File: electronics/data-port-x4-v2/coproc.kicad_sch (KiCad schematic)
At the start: 43 parts, among them U11 RP2354B, U12 AP2112K-3.3TRG1, Y2 ABM8-272-T3

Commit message: DATA x4 v2: the H5VU25UC ESD and 22 ohm USB resistors, two extended types fewer, re-routed
The user's "essaie les 3 premiers ?", via the orchestrator: two part
swaps, each an extended part type less in the panel order.

- R23/R24, the RP2354B's USB series resistors: 27 ohm (C25100,
  extended) -> 22 ohm 0402 (C25092, basic).  The RP2350's USB is Full
  Speed only: its driver's own impedance plus 22 ohm stays inside USB's
  28-44 ohm driver window, nearer its middle than 33 ohm.  Said in
  design.py.
- U4, U105...U406, the nine 4-line ESD arrays: TI TPD4E05U06DQAR
  (C138714) -> hongjiacheng H5VU25UC (C20615800, JLC "preferred
  extended": no Economic fee; $0.03 against $0.08).
  - On its own DFN2510-10L land (the tools commit before this).
  - The same pins; its 6/7/9/10 are tied inside to 5/4/2/1, so the
    flow-through lines keep one signal.
  - Its stand-off is 5 V (TI's 5.5 V).  Every line it guards stays at
    5 V or less: a DUT's pins at its VREF (<= 5 V), the lead's I2C and
    INT at 3.3 V.
- The land changed (rows 0.875 mm apart, longer pads, a GND bar), so
  the board is re-routed: Freerouting at 4 layers, no neckdown, with one
  hand-drawn via under the RP2354B's exposed pad (that run left the pad
  unfanned).  Of the variants tried in parallel, the one with a single
  pad via closed every link; with four, its buses can't pass under the
  pad.  ERC 0, DRC 0 (4 silk warnings), 0 unconnected, parity 0.
- CPL: all nine H5VU25UC land pin by pin within 0.005 mm, pin 1 on
  pin 1 (JLC_CPL_FIX 270 degrees).  3D: 209 bodies resolve.
- Regenerated:
  - both variants' BOM/CPL;
  - the order panel (DRC 0; each half matches its variant; mouse
    bites unchanged);
  - the viewer's GLBs (gltfpack);
  - jlc_parts.json (C20615800 and C25092 added, nothing refreshed);
  - the BOM outputs.
- tools/bom.py, recomputed by the cost session's own method (components
  at the snapshot's breaks x 1.12, which reproduces the old figures
  exactly; JLC's library tier, so the H5VU2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
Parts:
- R23, R24: value 27 -> 22; LCSC C25100 -> C25092; MPN 0402WGF270JTCE -> 0402WGF220JTCE
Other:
- note added: "12 MHz crystal (ABM8-272-T3, 15 pF, 1k on XOUT), USB on hub port 5 (22 Ω), RUN, BOOTSEL, LED, SWD"
- note removed: "12 MHz crystal (ABM8-272-T3, 15 pF, 1k on XOUT), USB on hub port 5 (27 Ω), RUN, BOOTSEL, LED, SWD"
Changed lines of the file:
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@@
 			)
 		)
-		(property "Value" "27"
+		(property "Value" "22"
 			(at 355.6 215.976 90)
 			(effects
@@
 			)
 		)
-		(property "Description" "Resistor 27 0402"
+		(property "Description" "Resistor 22 0402"
 			(at 355.6 213.36 0)
 			(effects
@@
 			)
 		)
-		(property "LCSC" "C25100"
+		(property "LCSC" "C25092"
 			(at 355.6 213.36 0)
 			(effects
@@
 			)
 		)
-		(property "MPN" "0402WGF270JTCE"
+		(property "MPN" "0402WGF220JTCE"
 			(at 355.6 213.36 0)
 			(effects
@@
 			)
 		)
-		(property "Value" "27"
+		(property "Value" "22"
 			(at 355.6 231.216 90)
 			(effects
@@
 			)
 		)
-		(property "Description" "Resistor 27 0402"
+		(property "Description" "Resistor 22 0402"
 			(at 355.6 228.6 0)
 			(effects
@@
 			)
 		)
-		(property "LCSC" "C25100"
+		(property "LCSC" "C25092"
 			(at 355.6 228.6 0)
 			(effects
@@
 			)
 		)
-		(property "MPN" "0402WGF270JTCE"
+		(property "MPN" "0402WGF220JTCE"
 			(at 355.6 228.6 0)
 			(effects
@@
 		)
 	)
-	(text "12 MHz crystal (ABM8-272-T3, 15 pF, 1k on XOUT), USB on hub port 5 (27 Ω), RUN, BOOTSEL, LED, SWD"
+	(text "12 MHz crystal (ABM8-272-T3, 15 pF, 1k on XOUT), USB on hub port 5 (22 Ω), RUN, BOOTSEL, LED, SWD"
 		(exclude_from_sim no)
 		(at 316.23 144.78 0)

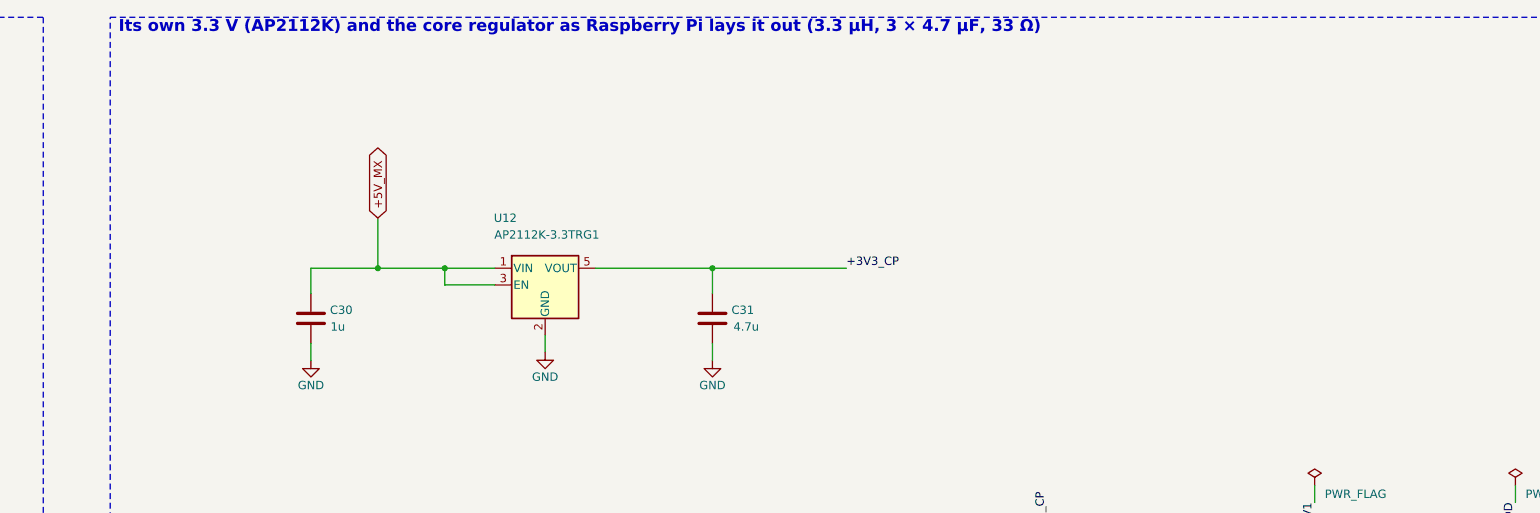
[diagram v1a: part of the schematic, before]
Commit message: DATA x4 v2: the usability review pass, layout B and a VBUS LED per port
One pass and one re-route for the usability review (docs/data-x4-logic-usability-review.md),
the user's go on layout B (2026-10-21):

- Layout B: one 2 × 6 per port, its pin names in two lines over it, the port number and the
  VBUS LED by its west end.  The headers sit 2 mm lower, at drawer z 28.5
  (rack.yaml › pcb.data_port_x4_v2.header), so the viewer's jumpers follow.
- A green VBUS LED per port (KT-0805G C2297 through 1k) on PORTn_5V_SW, before the shunt, so the
  INA226 doesn't count it.
- The LSF0108s' Vref_B/EN come from +5V_MX through 200k, not the port's VBUS, so each group is a
  voltage domain of its own.  The VREF dividers to the co-processor are 10k / 10k (were
  100k / 100k).  The bias current leaves by Vref_A: through 100k it would float an unwired VREF
  to about 2.1 V and the group would pass.  Through 10k it stays near 0.4 V, under the 0.65 V the
  LSF needs.  A board that is off isolates.
- The co-processor's AP2112K (U12) is out.  +3V3_CP comes from +3V3 through a 600 Ω ferrite
  (FB2, C1017).  U3 (AP2114H) then carries about 0.39 A, 0.66–0.75 W.
- Docs: the base solders two 2 × 1 pieces per port (GND/VREF, RESET/BOOT).

Re-routed with Freerouting (4 layers):
- ERC 0, copper DRC 0, 0 unconnected, parity 0.  The 4 silk-over-pad warnings are unchanged
  (U107–U407's marker on C105–C405).
- 216 3D models resolve.
- CPL: the new parts land within 0.1 mm rms, the LEDs placed by function.
- The cradle keep-outs clear by at least 0.67 mm: slots and latch, T-heads, rear band, boss.
  Checked in SolidCraft against the new STEP.

Regenerated:
- Both variants' BOM and CPL (base: 91 DNP).
- The order panel; its halves match their variants.
- The viewer GLBs and rack.json.

Cost, by the cost session's method in bom.py:
- The logic has 40 part types, 17 extended (was 41 and 18).
- The panel order of 2: $229.91 → $226.88 (−$3.03).
- Logic alone: $168.53 → $165.27.  Base alone: $84.50 → $8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
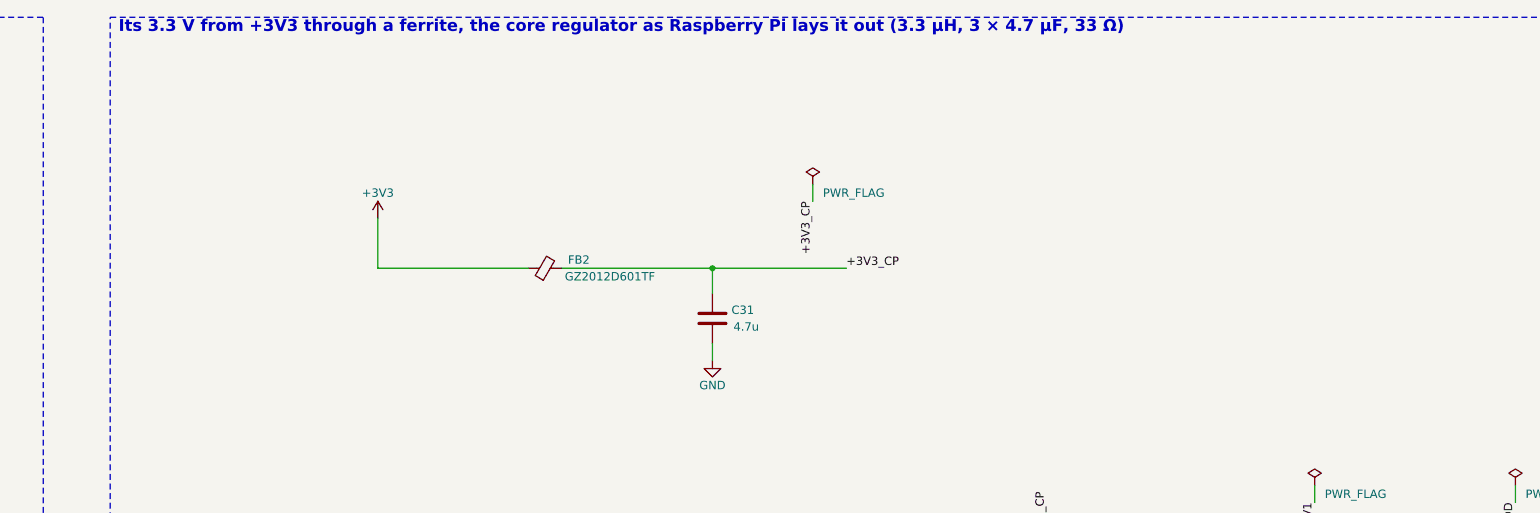
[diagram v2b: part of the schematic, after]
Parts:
- removed C30: 1u, Capacitor_SMD:C_0402_1005Metric, symbol Device:C
- removed U12: AP2112K-3.3TRG1, Package_TO_SOT_SMD:SOT-23-5, symbol Regulator_Linear:AP2112K-3.3
- added FB2: GZ2012D601TF, Inductor_SMD:L_0805_2012Metric, symbol Device:FerriteBead_Small
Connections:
- net +3V3: now also FB2.1
- net +3V3_CP: now also FB2.2
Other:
- note added: "Its 3.3 V from +3V3 through a ferrite, the core regulator as Raspberry Pi lays it out (3.3 µH, 3 × 4.7 µF, 33 Ω)"
- note removed: "Its own 3.3 V (AP2112K) and the core regulator as Raspberry Pi lays it out (3.3 µH, 3 × 4.7 µF, 33 Ω)"

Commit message: DATA x4 v2: datasheet audit fixes 1-9, conservative options, CFG_SEL 110
The DATA x4 v2 datasheet audit's fixes, approved by the user, plus the
conservative options that close U2, U8, U9 and U10:

- Core regulator (fixes 1-3).
  - L1 on a polarity-marked land: bench:L_Abracon_AOTA-B201610, RP's
    0.7 x 1.7 mm pads, the dot on pad 1 = +1V1 (U1's answer).
  - The block is Raspberry Pi's RP2350B Minimal R4-S1 one, turned 180
    degrees with U11, at their coordinates.  CIN and COUT sit on RP's
    0402 land (bench:C_0402_1005Metric_RP), so LX runs 0.3 mm between
    them.
  - Copper: their F.Cu areas (LX, +1V1 with the two V_OUT vias, PGND
    with its two vias, VIN) and their settings; VREG_FB taken at the
    V_OUT vias; CFILT on its own via.
  - The F.Cu GND pour leaves a hole round the block, so PGND meets the
    main GND only through its two vias.  No copper under LX and L1 on
    In1, In2 and B.Cu.
- Fix 4: C47 (DVDD pin 32) 100 nF -> 4.7 uF.
- Fix 5: R40 47k -> 10k, so GPIO45 stays >= -0.48 V; formula updated.
- Fix 6: UMW MAX809S (U5, C347371) drives the hub's RESET_N in place of
  R2/C6; C6 is its 100 nF.
- Fix 7: two H5VU25UC per port in flow-through.  VREF and RESET/BOOT
  sit at the header's two ends, so one part per end:
  - U108-U408 take VREF (logic only);
  - U109-U409 take RESET_N/BOOT_N with the 1k right behind them, fitted
    on the base too (schematic review N4).
  VREF and ports 1-3's RESET_N are drawn into their ESD pins; all 12
  lines checked in flow-through.
- Fixes 8, 9: the VREF isolation wording and the firmware rule (switches
  open below 0.65 V, in multi-dut-node.md); +5V_MX ~1-4 mA, FB1 and U3
  stale lines gone.
- Conservative options:
  - U2: R10 1M across XI-XO (C26083);
  - U8: R115-R415 100k in series with GPIO40-43;
  - U9: R11, R12 10k on the TCA6408A RESETs;
  - U10: C7, C8 4.7 uF.
- Hub on CFG_SEL 110, internal defaults with straps disabled (U11, U12
  answered by the user).  CFG_SEL1 and CFG_SEL2 pull up through their
  RN2/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
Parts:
- C32, C33: footprint Capacitor_SMD:C_0402_1005Metric -> bench:C_0402_1005Metric_RP
- C47: value 100n -> 4.7u; LCSC C1525 -> C23733; MPN CL05B104KO5NNNC -> CL05A475MP5NRNC
- L1: footprint Inductor_SMD:L_Murata_DFE201610P -> bench:L_Abracon_AOTA-B201610
- R40: value 47k -> 10k; LCSC C25792 -> C25744; MPN 0402WGF4702TCE -> 0402WGF1002TCE
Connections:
- net +1V1: now also L1.1; no longer L1.2
- net CP_VREG_LX: now also L1.2; no longer L1.1
- net CP_VREF1 renamed CP_ADC1
- net CP_VREF2 renamed CP_ADC2
- net CP_VREF3 renamed CP_ADC3
- net CP_VREF4 renamed CP_ADC4
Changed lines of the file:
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@@
 		)
 	)
-	(global_label "CP_VREF1"
+	(global_label "CP_ADC1"
 		(shape bidirectional)
 		(at 124.46 210.82 180)
@@
 		)
 	)
-	(global_label "CP_VREF2"
+	(global_label "CP_ADC2"
 		(shape bidirectional)
 		(at 124.46 213.36 180)
@@
 		)
 	)
-	(global_label "CP_VREF3"
+	(global_label "CP_ADC3"
 		(shape bidirectional)
 		(at 124.46 215.9 180)
@@
 		)
 	)
-	(global_label "CP_VREF4"
+	(global_label "CP_ADC4"
 		(shape bidirectional)
 		(at 124.46 218.44 180)
@@
 			)
 		)
-		(property "Footprint" "Inductor_SMD:L_Murata_DFE201610P"
+		(property "Footprint" "bench:L_Abracon_AOTA-B201610"
 			(at 345.44 106.68 0)
 			(effects
@@
 			)
 		)
-		(property "Description" "3.3 µH 2.4 A molded inductor, 0806, polarity dot (RP2350 core regulator)"
+		(property "Description" "3.3 µH 2.4 A molded inductor, 0806, polarity dot on pad 1 (RP2350 core regulator)"
 			(at 345.44 106.68 0)
 			(effects
@@
 		)
 	)
-	(label "CP_VREG_LX"
+	(label "+1V1"
 		(at 339.09 106.68 180)
 		(fields_autoplaced yes)
@@
 		)
 	)
-	(label "+1V1"
+	(label "CP_VREG_LX"
 		(at 351.79 106.68 0)
 		(fields_autoplaced yes)
@@
 			)
 		)
-		(property "Footprint" "Capacitor_SMD:C_0402_1005Metric"
+		(property "Footprint" "bench:C_0402_1005Metric_RP"
 			(at 457.2 111.76 0)
 			(effects
@@
 			)
 		)
-		(property "Footprint" "Capacitor_SMD:C_0402_1005Metric"
+		(property "Footprint" "bench:C_0402_1005Metric_RP"
 			(at 370.84 111.76 0)
 			(effects
@@
 			)
 		)
-		(property "Value" "100n"
+		(property "Value" "4.7u"
 			(at 208.332 62.23 0)
 			(effects
@@
 			)
 		)
-		(property "Description" "Capacitor 100n 0402"
+		(property "Description" "Capacitor 4.7u 0402"
 			(at 203.2 60.96 0)
 			(effects
@@
 			)
 		)
-		(property "LCSC" "C1525"
+		(property "LCSC" "C23733"
 			(at 203.2 60.96 0)
 			(effects
@@
 			)
 		)
-		(property "MPN" "CL05B104KO5NNNC"
+		(property "MPN" "CL05A475MP5NRNC"
 			(at 203.2 60.96 0)
 			(effects
@@
 			)
 		)
-		(property "Value" "47k"
+		(property "Value" "10k"
 			(at 542.071 300.99 0)
 			(effects
@@
 			)
 		)
-		(property "Description" "Resistor 47k 0402"
+		(property "Description" "Resistor 10k 0402"
 			(at 538.48 299.72 0)
 			(effects
@@
 			)
 		)
-		(property "LCSC" "C25792"
+		(property "LCSC" "C25744"
 			(at 538.48 299.72 0)
 			(effects
@@
 			)
 		)
-		(property "MPN" "0402WGF4702TCE"
+		(property "MPN" "0402WGF1002TCE"
 			(at 538.48 299.72 0)
 			(effects
@@
 		)
 	)
-	(text_box "GPIO2–9 = buses A–H (gusmanb CH1–8, 8-bit mode); GPIO0 → GPIO1 bridged (its trigger path).\nGPIO14 = the node's mark (TCA9534A P7); GPIO25 = LED; GPIO19…16, 13…10 = pull-up enables A…H (2.2k);\nGPIO40–43 = VREF 1–4 / 2; GPIO44 = +5V × 47/147; GPIO45 = 3.3 V − (3.3 + 5) × 47/147 from −5 V.\nRUN pulled up, BOOTSEL (QSPI_SS) through 1k: both held by the node (TCA9534A), open drain.\nCore regulator: L1 polarity dot towards VREG_LX; C32, C33, C34 and L1 as close as the Pico 2's."
+	(text_box "GPIO2–9 = buses A–H (gusmanb CH1–8, 8-bit mode); GPIO0 → GPIO1 bridged (its trigger path).\nGPIO14 = the node's mark (TCA9534A P7); GPIO25 = LED; GPIO19…16, 13…10 = pull-up enables A…H (2.2k);\nGPIO40–43 = VREF 1–4 / 2 (through 100k); GPIO44 = +5V × 47/147;\n  GPIO45 = 3.3 V − (3.3 + 5) × 10/110 from −5 V (2.55 V nominal).\nRUN pulled up, BOOTSEL (QSPI_SS) through 1k: both held by the node (TCA9534A), open drain.\nCore regulator: Raspberry Pi's Minimal R4 block turned 180°; L1's dot (pad 1) on +1V1, not VREG_LX.\nC47 (DVDD pin 32, furthest from the regulator) 4.7 µF; no copper under LX / L1 (In1, In2, B.Cu)."
 		(exclude_from_sim no)
 		(at 15.24 314.96 0)
-		(size 284.48 16.51)
+		(size 284.48 20.32)
 		(margins 1.5 1.5 1.5 1.5)
 		(stroke
